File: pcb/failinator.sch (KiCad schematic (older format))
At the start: 5 parts, among them P1 CONN_01X04, P4 CONN_01X06, U2 RASPIPLUSHEADER, U3 LDS-CD16RI, U4 LDS-CD16RI

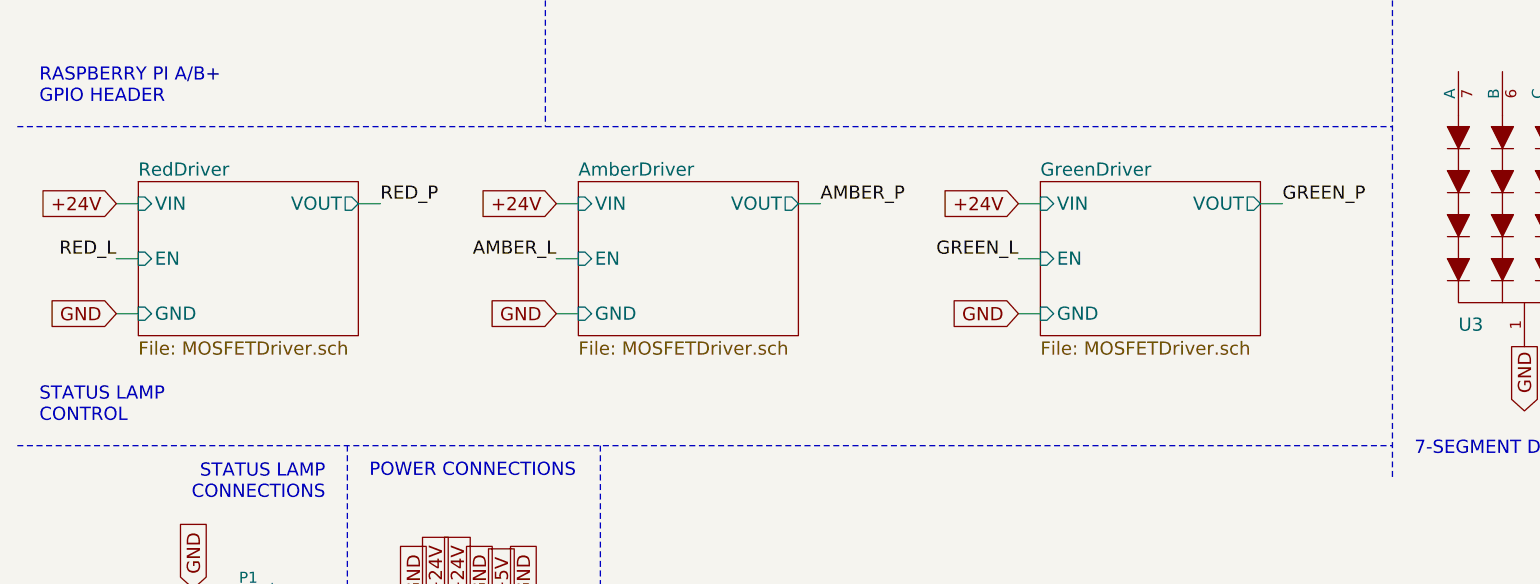
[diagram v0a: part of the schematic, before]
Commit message: Tweak layout of the "Status Lamp Control" area
Just a minor cosmetic tweak to improve the visual balance.
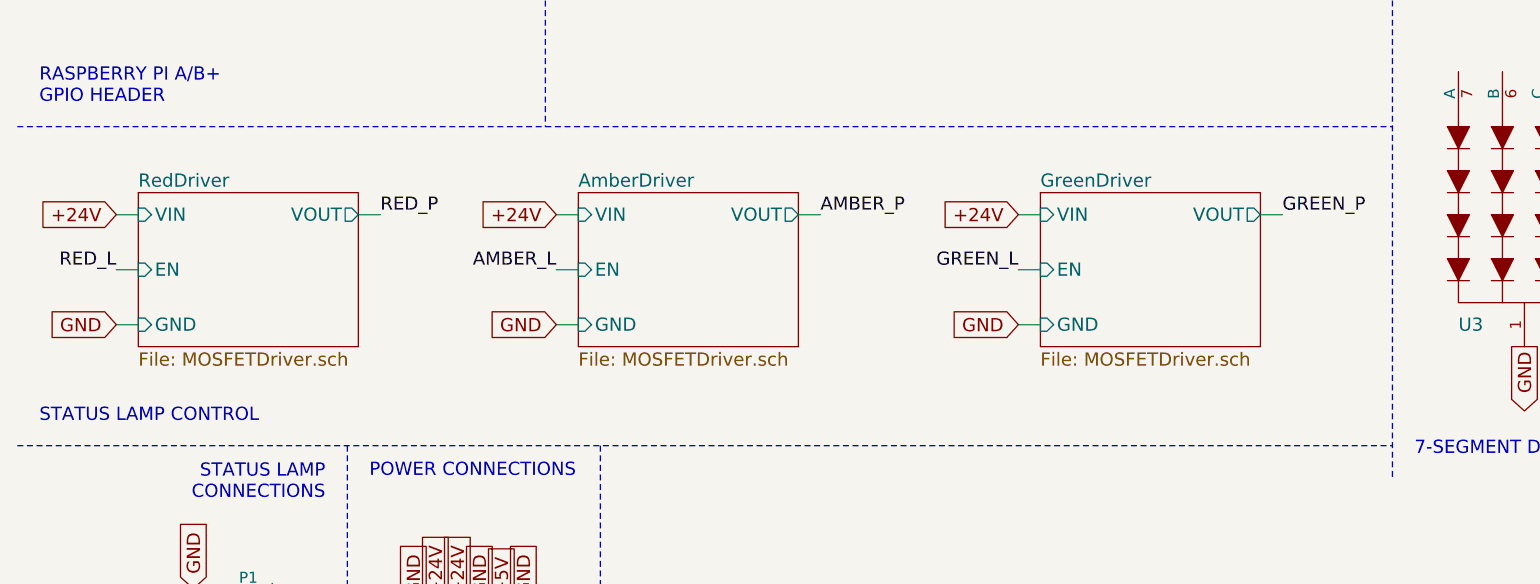
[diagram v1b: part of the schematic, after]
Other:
- note added: "STATUS LAMP CONTROL"
- note removed: "STATUS LAMP\nCONTROL"
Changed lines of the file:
@@
 Wire Wire Line
 	1350 7550 1400 7550
-Text GLabel 1000 5950 0    60   Input ~ 0
+Text GLabel 1000 6000 0    60   Input ~ 0
 GND
-Text GLabel 1000 5450 0    60   Input ~ 0
+Text GLabel 1000 5500 0    60   Input ~ 0
 +24V
-Text Label 1000 5700 2    60   ~ 0
+Text Label 1000 5750 2    60   ~ 0
 RED_L
-Text Label 2200 5450 0    60   ~ 0
+Text Label 2200 5500 0    60   ~ 0
 RED_P
-Text GLabel 3000 5950 0    60   Input ~ 0
+Text GLabel 3000 6000 0    60   Input ~ 0
 GND
-Text GLabel 3000 5450 0    60   Input ~ 0
+Text GLabel 3000 5500 0    60   Input ~ 0
 +24V
-Text Label 3000 5700 2    60   ~ 0
+Text Label 3000 5750 2    60   ~ 0
 AMBER_L
-Text Label 4200 5450 0    60   ~ 0
+Text Label 4200 5500 0    60   ~ 0
 AMBER_P
-Text GLabel 5100 5950 0    60   Input ~ 0
+Text GLabel 5100 6000 0    60   Input ~ 0
 GND
-Text GLabel 5100 5450 0    60   Input ~ 0
+Text GLabel 5100 5500 0    60   Input ~ 0
 +24V
-Text Label 5100 5700 2    60   ~ 0
+Text Label 5100 5750 2    60   ~ 0
 GREEN_L
-Text Label 6300 5450 0    60   ~ 0
+Text Label 6300 5500 0    60   ~ 0
 GREEN_P
 Wire Notes Line
@@
 STATUS LAMP\nCONNECTIONS
 Text Notes 650  6450 0    60   ~ 0
-STATUS LAMP\nCONTROL
+STATUS LAMP CONTROL
 $Comp
 L CONN_01X06 P4
@@
 POWER CONNECTIONS
 $Sheet
-S 1100 5350 1000 700
+S 1100 5400 1000 700
 U 568778A1
 F0 "RedDriver" 60
 F1 "MOSFETDriver.sch" 60
-F2 "VIN" I L 1100 5450 60
-F3 "GND" I L 1100 5950 60
-F4 "EN" I L 1100 5700 60
-F5 "VOUT" O R 2100 5450 60
+F2 "VIN" I L 1100 5500 60
+F3 "GND" I L 1100 6000 60
+F4 "EN" I L 1100 5750 60
+F5 "VOUT" O R 2100 5500 60
 $EndSheet
 Wire Wire Line
-	2100 5450 2200 5450
+	2100 5500 2200 5500
 Wire Wire Line
-	1000 5450 1100 5450
+	1000 5500 1100 5500
 Wire Wire Line
-	1000 5700 1100 5700
+	1000 5750 1100 5750
 Wire Wire Line
-	1000 5950 1100 5950
+	1000 6000 1100 6000
 $Sheet
-S 3100 5350 1000 700
+S 3100 5400 1000 700
 U 56879543
 F0 "AmberDriver" 60
 F1 "MOSFETDriver.sch" 60
-F2 "VIN" I L 3100 5450 60
-F3 "GND" I L 3100 5950 60
-F4 "EN" I L 3100 5700 60
-F5 "VOUT" O R 4100 5450 60
+F2 "VIN" I L 3100 5500 60
+F3 "GND" I L 3100 6000 60
+F4 "EN" I L 3100 5750 60
+F5 "VOUT" O R 4100 5500 60
 $EndSheet
 $Sheet
-S 5200 5350 1000 700
+S 5200 5400 1000 700
 U 5687AB7C
 F0 "GreenDriver" 60
 F1 "MOSFETDriver.sch" 60
-F2 "VIN" I L 5200 5450 60
-F3 "GND" I L 5200 5950 60
-F4 "EN" I L 5200 5700 60
-F5 "VOUT" O R 6200 5450 60
+F2 "VIN" I L 5200 5500 60
+F3 "GND" I L 5200 6000 60
+F4 "EN" I L 5200 5750 60
+F5 "VOUT" O R 6200 5500 60
 $EndSheet
 Wire Wire Line
-	3000 5450 3100 5450
+	3000 5500 3100 5500
 Wire Wire Line
-	3000 5700 3100 5700
+	3000 5750 3100 5750
 Wire Wire Line
-	3000 5950 3100 5950
+	3000 6000 3100 6000
 Wire Wire Line
-	4100 5450 4200 5450
+	4100 5500 4200 5500
 Wire Wire Line
-	5100 5450 5200 5450
+	5100 5500 5200 5500
 Wire Wire Line
-	5100 5700 5200 5700
+	5100 5750 5200 5750
 Wire Wire Line
-	5100 5950 5200 5950
+	5100 6000 5200 6000
 Wire Wire Line
-	6200 5450 6300 5450
+	6200 5500 6300 5500
 Wire Notes Line
 	2950 600  2950 5100

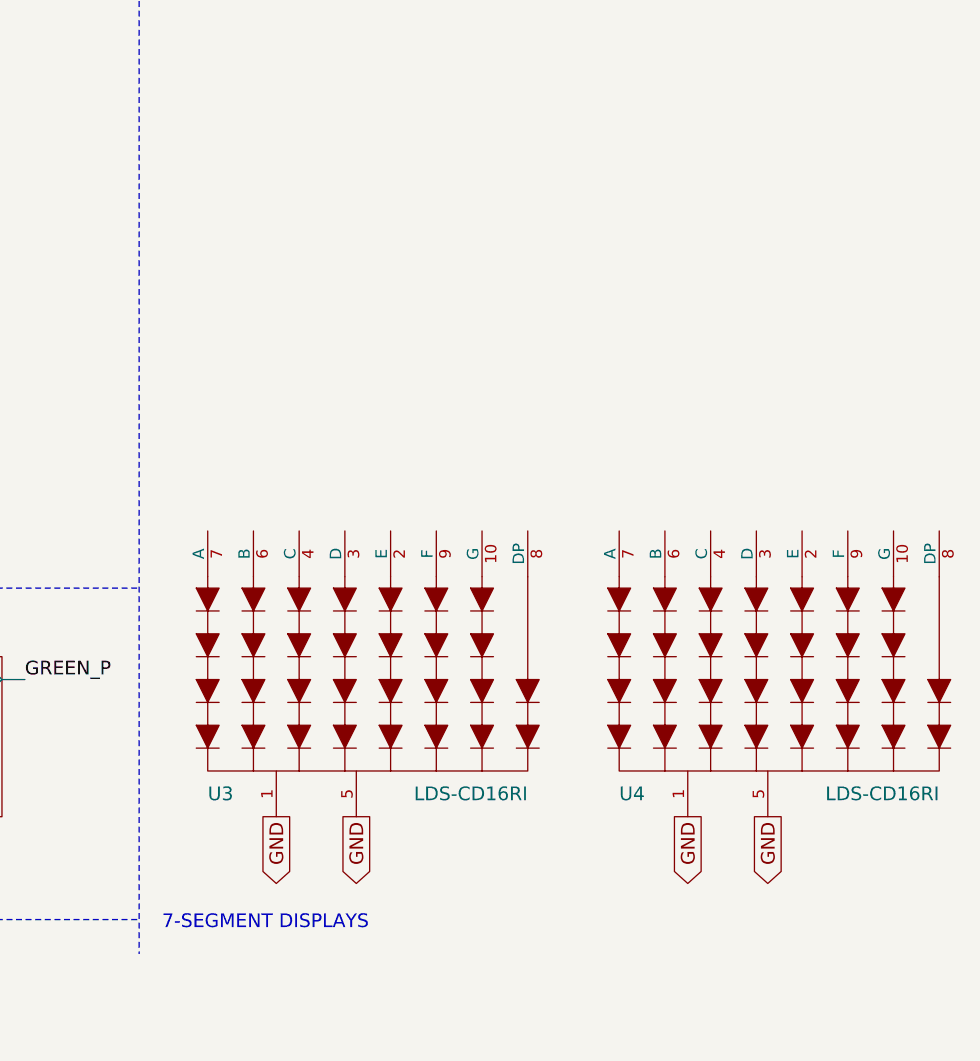
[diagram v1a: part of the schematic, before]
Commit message: MOSFET driver circuits for the 7-segment displays
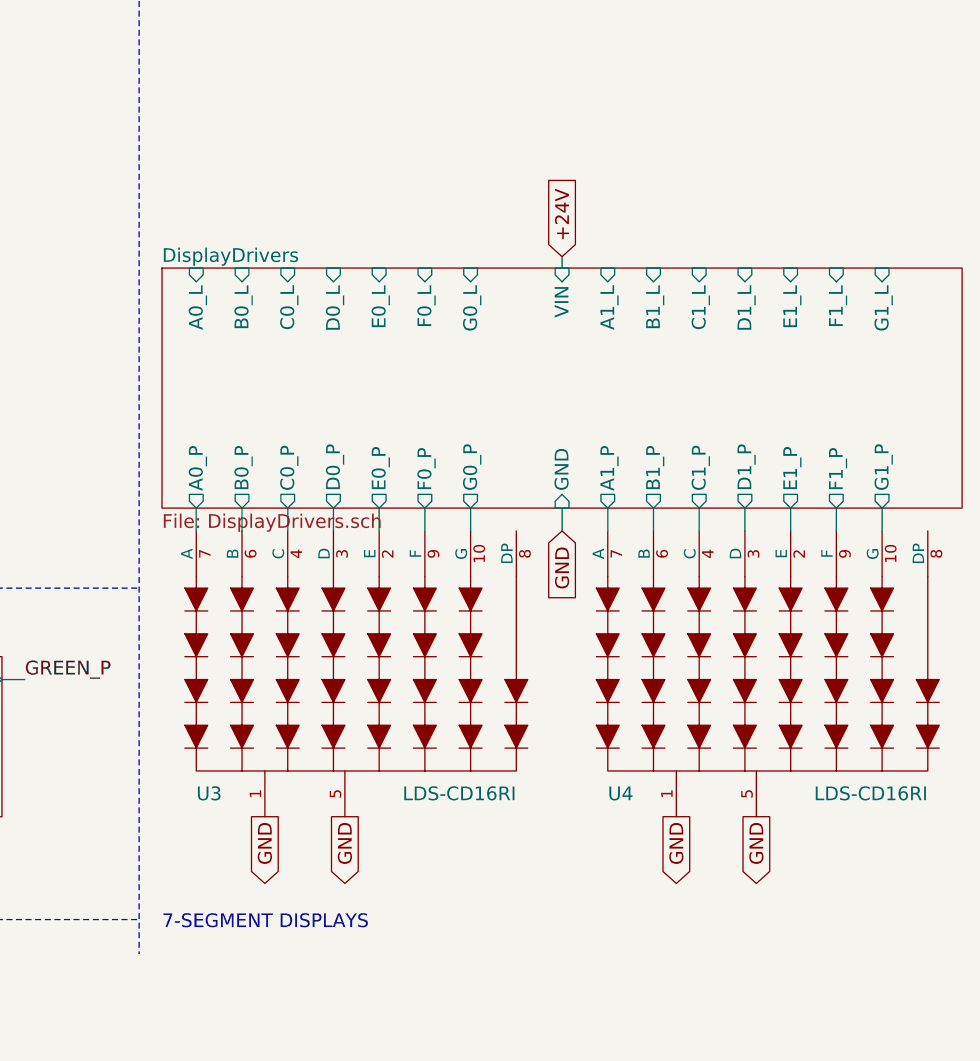
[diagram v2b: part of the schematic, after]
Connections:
- net DisplayDrivers/G0_P: now reaches U3.10 (G)
- net DisplayDrivers/E0_P: now reaches U3.2 (E)
- net DisplayDrivers/D0_P: now reaches U3.3 (D)
- net DisplayDrivers/C0_P: now reaches U3.4 (C)
- net DisplayDrivers/B0_P: now reaches U3.6 (B)
- net DisplayDrivers/A0_P: now reaches U3.7 (A)
- net DisplayDrivers/F0_P: now reaches U3.9 (F)
- net DisplayDrivers/G1_P: now reaches U4.10 (G)
- net DisplayDrivers/E1_P: now reaches U4.2 (E)
- net DisplayDrivers/D1_P: now reaches U4.3 (D)
- net DisplayDrivers/C1_P: now reaches U4.4 (C)
- net DisplayDrivers/B1_P: now reaches U4.6 (B)
- net DisplayDrivers/A1_P: now reaches U4.7 (A)
- net DisplayDrivers/F1_P: now reaches U4.9 (F)
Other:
- moved on the sheet: U3, U4
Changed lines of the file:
@@
 $Descr USLetter 11000 8500
 encoding utf-8
-Sheet 1 4
+Sheet 1 19
 Title "Failinator"
 Date ""
@@
 L LDS-CD16RI U3
 U 1 1 5688764B
-P 7800 5450
-F 0 "U3" H 7100 4900 60  0000 L CNN
-F 1 "LDS-CD16RI" H 8500 4900 60  0000 R CNN
-F 2 "" H 7550 5850 60  0000 C CNN
-F 3 "" H 7550 5850 60  0000 C CNN
-	1    7800 5450
+P 7750 5450
+F 0 "U3" H 7050 4900 60  0000 L CNN
+F 1 "LDS-CD16RI" H 8450 4900 60  0000 R CNN
+F 2 "" H 7500 5850 60  0000 C CNN
+F 3 "" H 7500 5850 60  0000 C CNN
+	1    7750 5450
 	1    0    0    -1
 $EndComp
-Text GLabel 7400 6100 3    60   Output ~ 0
-GND
-Text GLabel 7750 6100 3    60   Output ~ 0
+Text GLabel 7350 6100 3    60   Output ~ 0
+GND
+Text GLabel 7700 6100 3    60   Output ~ 0
 GND
 $Comp
 L LDS-CD16RI U4
 U 1 1 56887D47
-P 9600 5450
-F 0 "U4" H 8900 4900 60  0000 L CNN
-F 1 "LDS-CD16RI" H 10300 4900 60  0000 R CNN
-F 2 "" H 9350 5850 60  0000 C CNN
-F 3 "" H 9350 5850 60  0000 C CNN
-	1    9600 5450
+P 9550 5450
+F 0 "U4" H 8850 4900 60  0000 L CNN
+F 1 "LDS-CD16RI" H 10250 4900 60  0000 R CNN
+F 2 "" H 9300 5850 60  0000 C CNN
+F 3 "" H 9300 5850 60  0000 C CNN
+	1    9550 5450
 	1    0    0    -1
 $EndComp
-Text GLabel 9200 6100 3    60   Output ~ 0
-GND
-Text GLabel 9550 6100 3    60   Output ~ 0
+Text GLabel 9150 6100 3    60   Output ~ 0
+GND
+Text GLabel 9500 6100 3    60   Output ~ 0
 GND
 Text Notes 6900 6600 0    60   ~ 0
@@
 Wire Wire Line
 	2400 2050 2350 2050
+Text GLabel 8650 4850 3    60   Input ~ 0
+GND
+Text GLabel 8650 3650 1    60   Input ~ 0
++24V
+$Sheet
+S 6900 3700 3500 1050
+U 5694859C
+F0 "DisplayDrivers" 60
+F1 "DisplayDrivers.sch" 60
+F2 "VIN" I T 8650 3700 60
+F3 "GND" I B 8650 4750 60
+F4 "A0_L" I T 7050 3700 60
+F5 "B0_L" I T 7250 3700 60
+F6 "C0_L" I T 7450 3700 60
+F7 "D0_L" I T 7650 3700 60
+F8 "E0_L" I T 7850 3700 60
+F9 "F0_L" I T 8050 3700 60
+F10 "G0_L" I T 8250 3700 60
+F11 "A0_P" O B 7050 4750 60
+F12 "B0_P" O B 7250 4750 60
+F13 "C0_P" O B 7450 4750 60
+F14 "D0_P" O B 7650 4750 60
+F15 "E0_P" O B 7850 4750 60
+F16 "F0_P" O B 8050 4750 60
+F17 "G0_P" O B 8250 4750 60
+F18 "A1_L" I T 8850 3700 60
+F19 "B1_L" I T 9050 3700 60
+F20 "C1_L" I T 9250 3700 60
+F21 "D1_L" I T 9450 3700 60
+F22 "E1_L" I T 9650 3700 60
+F23 "F1_L" I T 9850 3700 60
+F24 "G1_L" I T 10050 3700 60
+F25 "A1_P" O B 8850 4750 60
+F26 "B1_P" O B 9050 4750 60
+F27 "C1_P" O B 9250 4750 60
+F28 "D1_P" O B 9450 4750 60
+F29 "E1_P" O B 9650 4750 60
+F30 "F1_P" O B 9850 4750 60
+F31 "G1_P" O B 10050 4750 60
+$EndSheet
+Wire Wire Line
+	7050 4750 7050 4850
+Wire Wire Line
+	7250 4750 7250 4850
+Wire Wire Line
+	7450 4750 7450 4850
+Wire Wire Line
+	7650 4750 7650 4850
+Wire Wire Line
+	7850 4750 7850 4850
+Wire Wire Line
+	8050 4750 8050 4850
+Wire Wire Line
+	8250 4750 8250 4850
+Wire Wire Line
+	8650 4750 8650 4850
+Wire Wire Line
+	8850 4750 8850 4850
+Wire Wire Line
+	9050 4750 9050 4850
+Wire Wire Line
+	9250 4750 9250 4850
+Wire Wire Line
+	9450 4750 9450 4850
+Wire Wire Line
+	9650 4750 9650 4850
+Wire Wire Line
+	9850 4750 9850 4850
+Wire Wire Line
+	10050 4750 10050 4850
+Wire Wire Line
+	8650 3650 8650 3700
 $EndSCHEMATC
